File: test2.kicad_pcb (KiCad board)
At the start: 2 copper layers, 42 parts, among them Q1 IRLZ34N, Q2 IRLZ34N, Q3 IRLZ34N, Q4 IRLZ34N, Q5 IRLZ34N, Q6 IRLZ34N, Q7 IRLZ34N, Q8 IRLZ34N, U1 TEENSY3.1, U10 HCPL3120, U2 HCPL3120, U3 TRACO_TEL_DCDC, U4 HCPL3120, U5 HCPL3120, U6 HCPL3120, U7 HCPL3120, U8 HCPL3120, U9 HCPL3120

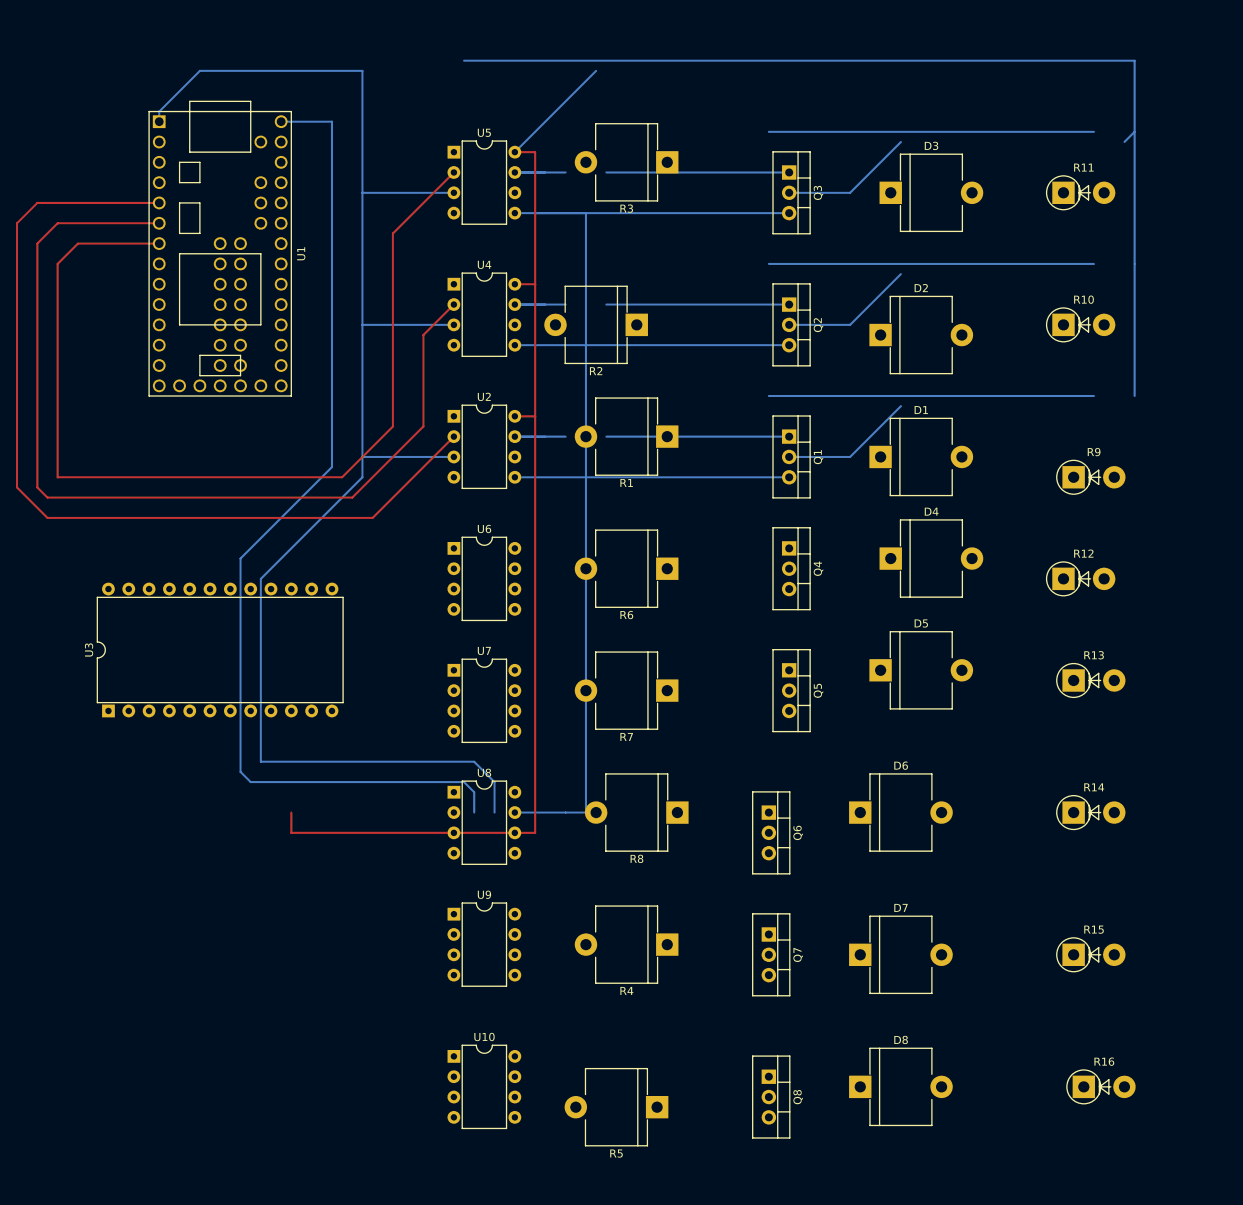
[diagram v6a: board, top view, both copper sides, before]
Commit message: much neater layout :) but only sorted the first 3 chanels, but the concept works
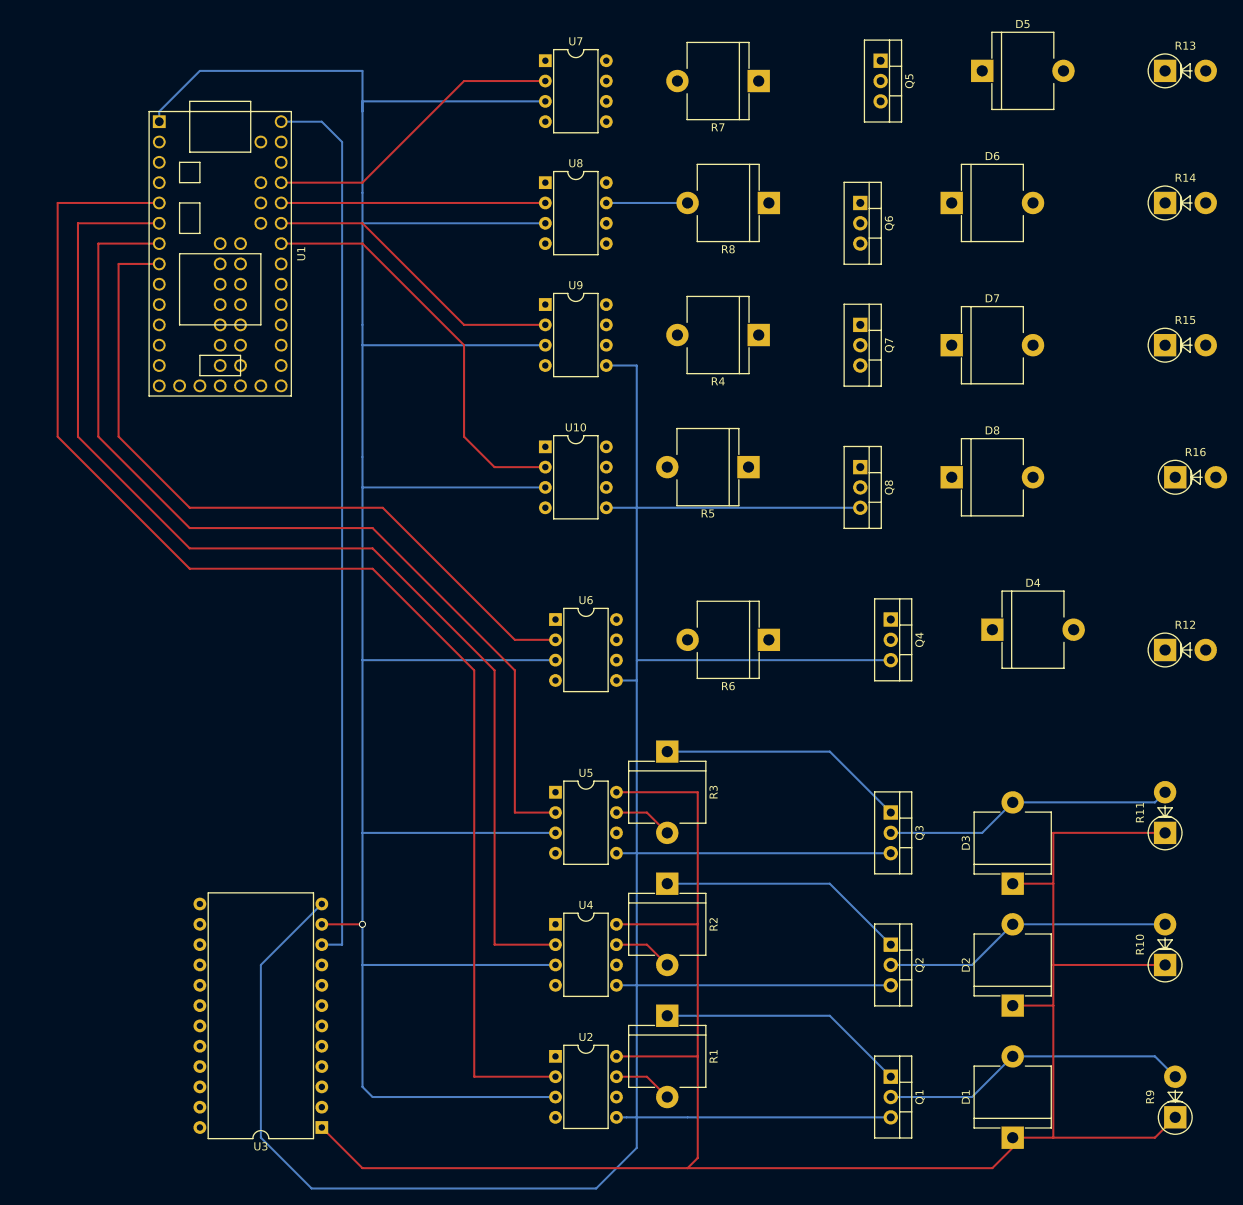
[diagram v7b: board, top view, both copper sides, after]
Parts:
- moved D3 87.7 mm to (148.6, 149.9), turned to 90 degrees
- moved D1 86.7 mm to (148.6, 181.6), turned to 90 degrees
- moved D2 85.4 mm to (148.6, 165.1), turned to 90 degrees
- moved U5 81.0 mm to (91.4, 138.4)
- moved Q1 81.0 mm to (133.3, 174.0)
- moved R10 81.0 mm to (167.6, 160.0), turned to 90 degrees
- moved U2 81.0 mm to (91.4, 171.4)
- moved U4 81.0 mm to (91.4, 154.9)
- moved Q2 81.0 mm to (133.3, 157.5)
- moved Q3 81.0 mm to (133.3, 141.0)
- moved R11 81.0 mm to (167.6, 143.5), turned to 90 degrees
- moved R9 81.0 mm to (168.9, 179.1), turned to 90 degrees
- moved R5 80.8 mm to (115.6, 97.8)
- moved U8 77.1 mm to (90.2, 62.2)
- moved D6 77.1 mm to (141.0, 64.8)
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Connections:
- Q4 pad 3: (no net) -> GND
- U1 pad 10: (no net) -> Net-(U1-Pad10)
- U1 pad 11: (no net) -> Net-(U1-Pad11)
- U1 pad 12: (no net) -> Net-(U1-Pad12)
- U1 pad 13: (no net) -> Net-(U1-Pad13)
- U1 pad 14: (no net) -> Net-(U1-Pad14)
- U1 pad 15: (no net) -> Net-(U1-Pad15)
- U1 pad 16: (no net) -> Net-(U1-Pad16)
- U1 pad 17: (no net) -> Net-(U1-Pad17)
- U1 pad 18: (no net) -> Net-(U1-Pad18)
- U1 pad 19: (no net) -> Net-(U1-Pad19)
- U1 pad 2: (no net) -> Net-(U1-Pad2)
- U1 pad 20: (no net) -> Net-(U1-Pad20)
- U1 pad 21: (no net) -> Net-(U1-Pad21)
- U1 pad 22: (no net) -> Net-(U1-Pad22)
- U1 pad 23: (no net) -> Net-(U1-Pad23)
- U1 pad 24: (no net) -> Net-(U1-Pad24)
- U1 pad 25: (no net) -> Net-(U1-Pad25)
- U1 pad 26: (no net) -> Net-(U1-Pad26)
- U1 pad 3: (no net) -> Net-(U1-Pad3)
- U1 pad 31: (no net) -> Net-(U1-Pad31)
- U1 pad 32: (no net) -> Net-(U1-Pad32)
- U1 pad 34: (no net) -> Net-(U1-Pad34)
- U1 pad 35: (no net) -> Net-(U1-Pad35)
- U1 pad 36: (no net) -> Net-(U1-Pad36)
- U1 pad 37: (no net) -> Net-(U1-Pad37)
- U1 pad 38: (no net) -> Net-(U1-Pad38)
- U1 pad 39: (no net) -> Net-(U1-Pad39)
- U1 pad 4: (no net) -> Net-(U1-Pad4)
- U1 pad 40: (no net) -> Net-(U1-Pad40)
- U1 pad 41: (no net) -> Net-(U1-Pad41)
- U1 pad 42: (no net) -> Net-(U1-Pad42)
- U1 pad 43: (no net) -> Net-(U1-Pad43)
- U1 pad 44: (no net) -> Net-(U1-Pad44)
- U1 pad 45: (no net) -> Net-(U1-Pad45)
- U1 pad 46: (no net) -> Net-(U1-Pad46)
- U1 pad 47: (no net) -> Net-(U1-Pad47)
- U1 pad 48: (no net) -> Net-(U1-Pad48)
- U1 pad 49: (no net) -> Net-(U1-Pad49)
- U1 pad 50: (no net) -> Net-(U1-Pad50)
- U1 pad 51: (no net) -> Net-(U1-Pad51)
- U1 pad 9: (no net) -> Net-(U1-Pad9)
- U10 pad 1: (no net) -> Net-(U10-Pad1)
- U10 pad 4: (no net) -> Net-(U10-Pad4)
- U10 pad 6: (no net) -> Net-(U10-Pad6)
- U2 pad 1: (no net) -> Net-(U2-Pad1)
- U2 pad 4: (no net) -> Net-(U2-Pad4)
- U2 pad 6: (no net) -> Net-(U2-Pad6)
- U3 pad 1: Net-(U1-Pad33) -> +24V
- U3 pad 10: +24V -> Net-(U1-Pad33)
- U3 pad 11: GND -> /Sheet58E8F73D/cleanGND
- U3 pad 12: /Sheet58E8F73D/cleanGND -> GND
- U4 pad 1: (no net) -> Net-(U4-Pad1)
- U4 pad 4: (no net) -> Net-(U4-Pad4)
- U4 pad 6: (no net) -> Net-(U4-Pad6)
- U5 pad 1: (no net) -> Net-(U5-Pad1)
- U5 pad 4: (no net) -> Net-(U5-Pad4)
- U5 pad 6: (no net) -> Net-(U5-Pad6)
- U6 pad 1: (no net) -> Net-(U6-Pad1)
- U6 pad 4: (no net) -> Net-(U6-Pad4)
- U6 pad 6: (no net) -> Net-(U6-Pad6)
- U7 pad 1: (no net) -> Net-(U7-Pad1)
- U7 pad 4: (no net) -> Net-(U7-Pad4)
- U7 pad 6: (no net) -> Net-(U7-Pad6)
- U8 pad 1: (no net) -> Net-(U8-Pad1)
- U8 pad 4: (no net) -> Net-(U8-Pad4)
- U8 pad 6: (no net) -> Net-(U8-Pad6)
- U9 pad 1: (no net) -> Net-(U9-Pad1)
- U9 pad 4: (no net) -> Net-(U9-Pad4)
- U9 pad 6: (no net) -> Net-(U9-Pad6)
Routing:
- net (no net): track 249.4 -> 0.00 mm
- net GND: track 151.1 -> 354.6 mm
- net /Sheet58E8F73D/cleanGND: track 188.8 -> 350.6 mm, vias 0 -> 1
- net +24V: track 140.1 -> 266.4 mm
- net /Sheet58E8F73D/chanel4: track 0.00 -> 91.8 mm
- net /Sheet58E8F73D/chanel1: track 112.2 -> 167.0 mm
- net /Sheet58E8F73D/chanel8: track 0.00 -> 51.3 mm
- net /Sheet58E8F73D/chanel7: track 0.00 -> 38.3 mm
- net /Sheet58E8F73D/changel5: track 0.00 -> 38.3 mm
- net /Sheet58E8F73D/chanel6: track 0.00 -> 33.0 mm
- net Net-(R8-Pad2): track 41.9 -> 8.89 mm
- net /Sheet58E8F73D/chanel2: track 116.1 -> 142.9 mm
- net Net-(D1-Pad2): track 16.6 -> 38.7 mm
- net Net-(D2-Pad2): track 16.6 -> 36.4 mm
- net Net-(D3-Pad2): track 16.6 -> 36.4 mm
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
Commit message: big board but dosent look tooo bad
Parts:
- added BT1: Battery, BoardEdgebattery:WSBattery, F.Cu at (146.1, 57.1)
- added Pressure1: POT, wsPot:Potentiometer_Trimmer_WS_Vertical_Px5.0mm_Py10.0mm, F.Cu at (71.1, 77.5)
- added Presure2: POT, wsPot:Potentiometer_Trimmer_WS_Vertical_Px5.0mm_Py10.0mm, F.Cu at (71.1, 96.5)
- added Presure3: POT, wsPot:Potentiometer_Trimmer_WS_Vertical_Px5.0mm_Py10.0mm, F.Cu at (71.1, 115.6)
- added Retract1: POT, wsPot:Potentiometer_Trimmer_WS_Vertical_Px5.0mm_Py10.0mm, F.Cu at (71.1, 172.7)
- added Spare1: POT, wsPot:Potentiometer_Trimmer_WS_Vertical_Px5.0mm_Py10.0mm, F.Cu at (71.1, 134.6)
- added Targeting1: POT, wsPot:Potentiometer_Trimmer_WS_Vertical_Px5.0mm_Py10.0mm, F.Cu at (71.1, 153.7)
- D1, D2, D3, D4, D5, D6, D7, D8: footprint Diodes_THT:D_5KP_P10.16mm_Horizontal -> Diodes_THT:D_A-405_P10.16mm_Horizontal
- Q1, Q2, Q3, Q4, Q5, Q6, Q7, Q8: footprint TO_SOT_Packages_THT:TO-220_Vertical -> TO_SOT_Packages_THT:TO-220_Horizontal
- R1, R2, R3, R4, R5, R6, R7, R8: footprint Diodes_THT:D_5KP_P10.16mm_Horizontal -> wsResistorNorm:R_Axial_DIN0207_L6.3mm_D2.5mm_P10.16mm_Horizontal
- R10, R11, R12, R13, R14, R15, R16, R9: footprint Diodes_THT:D_5W_P5.08mm_Vertical_AnodeUp -> wsValve:Value
- moved U9 59.1 mm to (142.2, 105.4)
- moved U10 58.5 mm to (142.2, 121.9)
- moved U8 58.5 mm to (142.2, 88.9)
- moved U7 57.9 mm to (142.2, 72.4)
- moved D6 57.1 mm to (186.7, 99.1), turned to 90 degrees
- moved D8 56.4 mm to (186.7, 132.1), turned to 90 degrees
- moved D7 56.4 mm to (186.7, 115.6), turned to 90 degrees
- moved U6 55.2 mm to (142.2, 138.4)
- moved D5 54.2 mm to (186.7, 82.5), turned to 90 degrees
- moved R3 53.4 mm to (156.2, 149.9)
- moved U2 53.4 mm to (142.2, 188.0)
- moved R1 53.4 mm to (156.2, 182.9)
- moved R2 53.4 mm to (156.2, 166.4)
- moved U4 53.4 mm to (142.2, 171.4)
- moved U5 53.4 mm to (142.2, 154.9)
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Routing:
- net +24V: track 266.4 -> 587.1 mm
- net Net-(Pressure1-Pad1): track 111.5 -> 285.4 mm
- net /Sheet58E8F73D/cleanGND: track 350.6 -> 515.8 mm
- net Net-(Retract1-Pad2): track 0.00 -> 114.7 mm
- net Net-(Targeting1-Pad2): track 0.00 -> 91.3 mm
- net Net-(Spare1-Pad2): track 0.00 -> 76.1 mm
- net Net-(Presure3-Pad2): track 0.00 -> 61.6 mm
- net Net-(Pressure1-Pad2): track 0.00 -> 60.5 mm
- net Net-(Presure2-Pad2): track 0.00 -> 54.6 mm
- net Net-(D7-Pad2): track 0.00 -> 33.6 mm
- net Net-(D5-Pad2): track 0.00 -> 33.6 mm
- net Net-(D8-Pad2): track 0.00 -> 33.6 mm
- net Net-(D6-Pad2): track 0.00 -> 33.6 mm
- net Net-(D4-Pad2): track 0.00 -> 33.6 mm
- net Net-(Q3-Pad1): track 31.1 -> 11.7 mm
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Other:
- board outline added: 141 x 158.8 mm
- board text added: "Point Blank Robot Wars preAlpha Derisk"
- board text added: "Point Blank Robot Wars version: preAlpha Derisk Board and Software: William Salmon"
